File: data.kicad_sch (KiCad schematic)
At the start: 37 parts, among them J3001 Conn_01x04, J6 USB_C_Receptacle_USB2.0, SW1 SWITCH-SPST, SW2 SWITCH-SPST, U27 RP2040, U3 TPS22919DCKR, U8 W25Q16JVUXIQ TR, U9 SK6812, Y1 12MHz

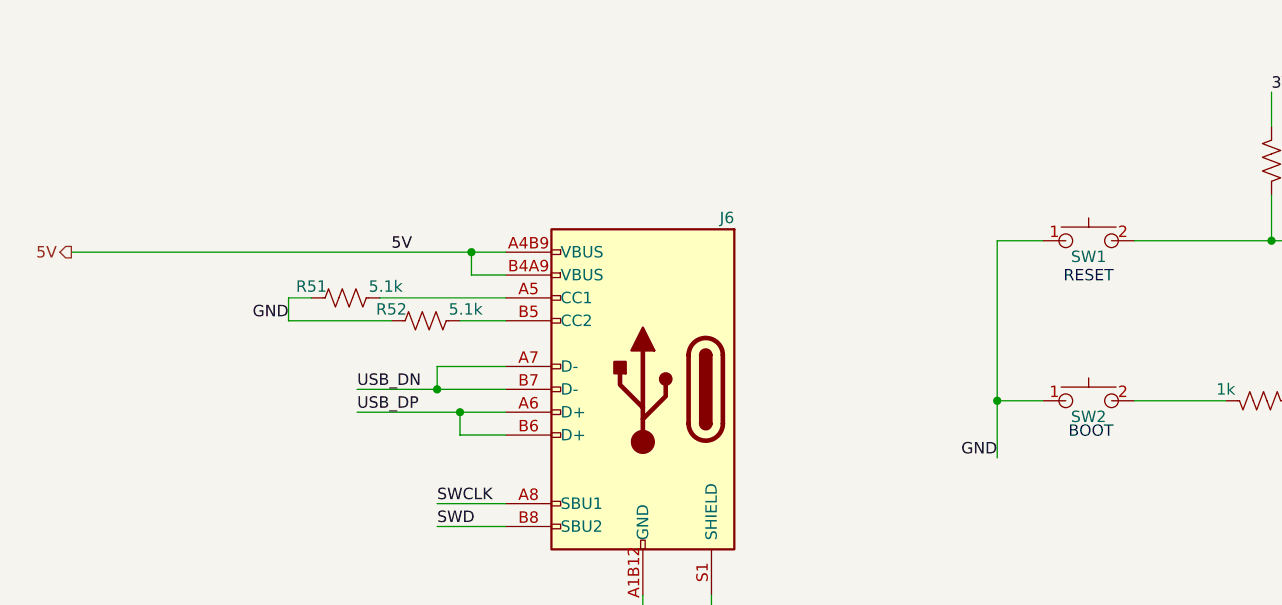
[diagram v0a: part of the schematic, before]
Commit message: started to piece in the BZM2 into schematic
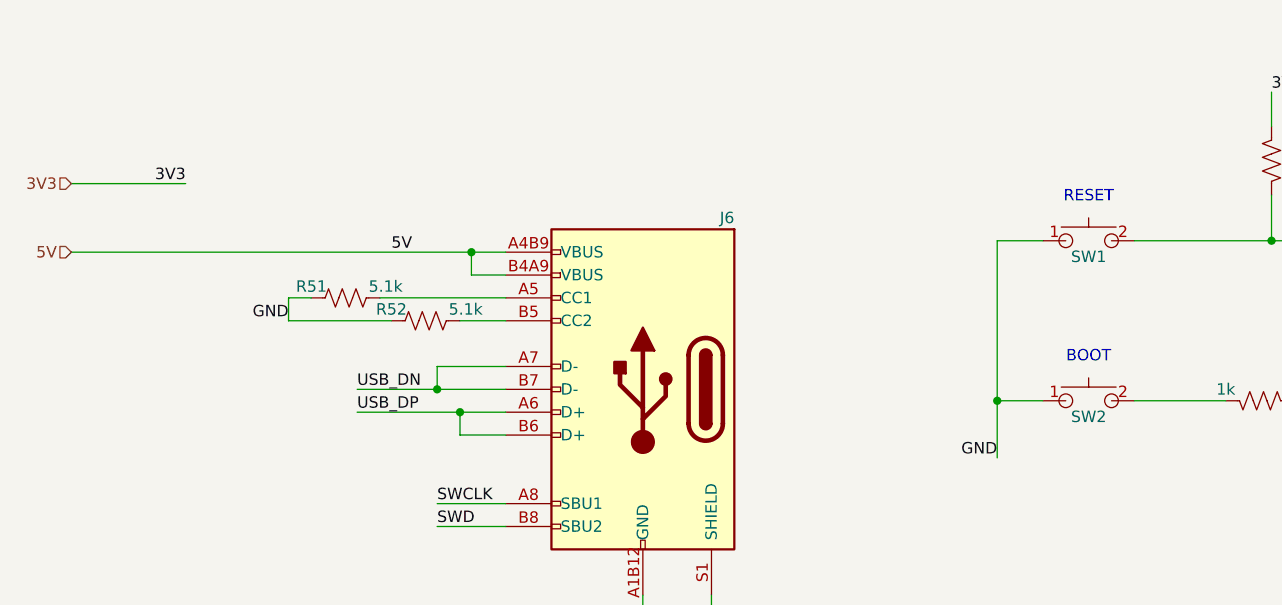
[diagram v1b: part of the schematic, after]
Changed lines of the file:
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@@
 	(text "BOOT"
 		(exclude_from_sim no)
-		(at 164.084 96.266 0)
+		(at 163.83 87.884 0)
 		(effects
 			(font
@@
 	(text "RESET"
 		(exclude_from_sim no)
-		(at 163.83 78.994 0)
+		(at 163.83 70.104 0)
 		(effects
 			(font
@@
 	(wire
 		(pts
+			(xy 50.8 68.58) (xy 63.5 68.58)
+		)
+		(stroke
+			(width 0)
+			(type default)
+		)
+	)
+	(wire
+		(pts
 			(xy 254 48.26) (xy 265.43 48.26)
 		)
@@
 			)
 			(justify left bottom)
+		)
+	)
+	(label "3V3"
+		(at 63.5 68.58 180)
+		(effects
+			(font
+				(size 1.27 1.27)
+			)
+			(justify right bottom)
 		)
 	)
@@
 	)
 	(hierarchical_label "5V"
-		(shape output)
+		(shape input)
 		(at 50.8 76.2 180)
 		(effects
 			(font
+				(size 1.27 1.27)
+			)
+			(justify right)
+		)
+	)
+	(hierarchical_label "3V3"
+		(shape input)
+		(at 50.8 68.58 180)
+		(effects
+			(font

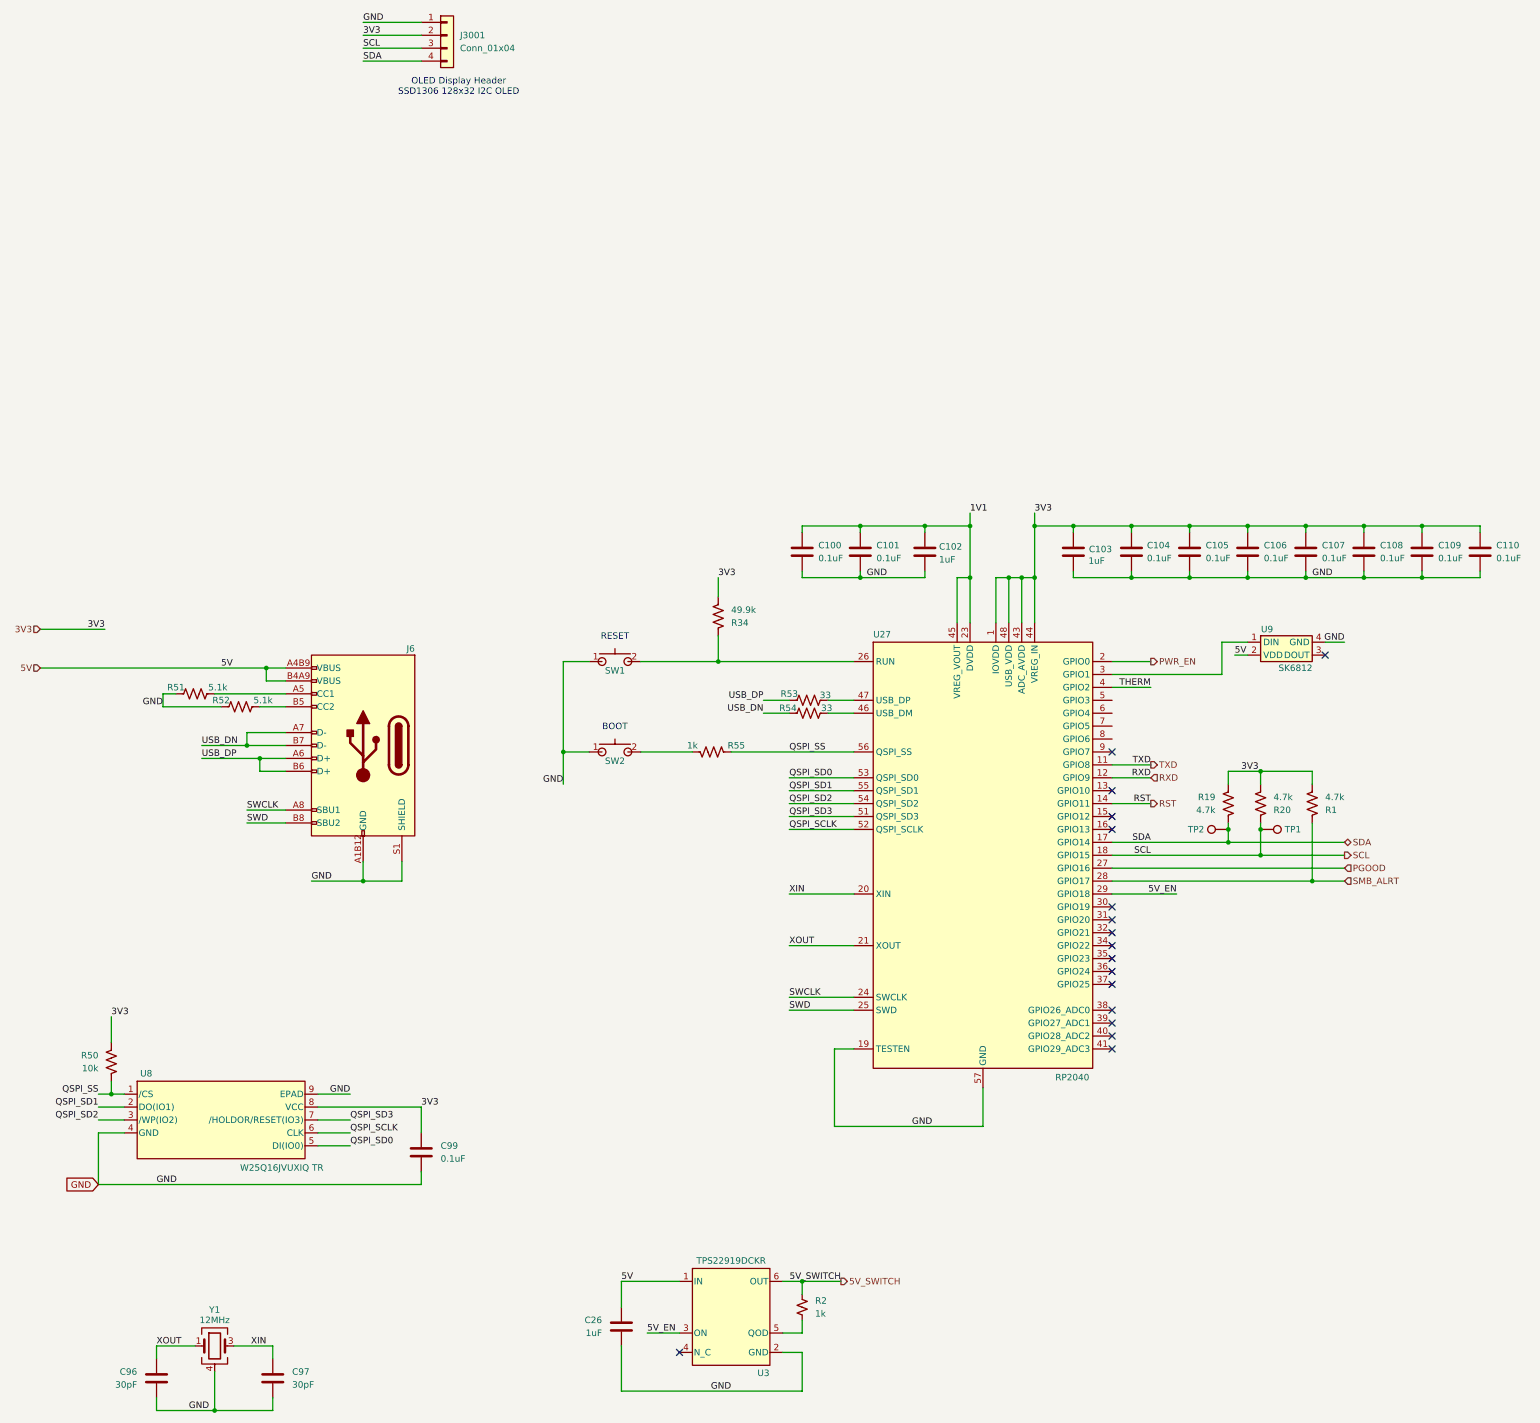
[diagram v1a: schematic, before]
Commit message: finished adding ASICs to schematic. Change VR to single phase 2.8V output
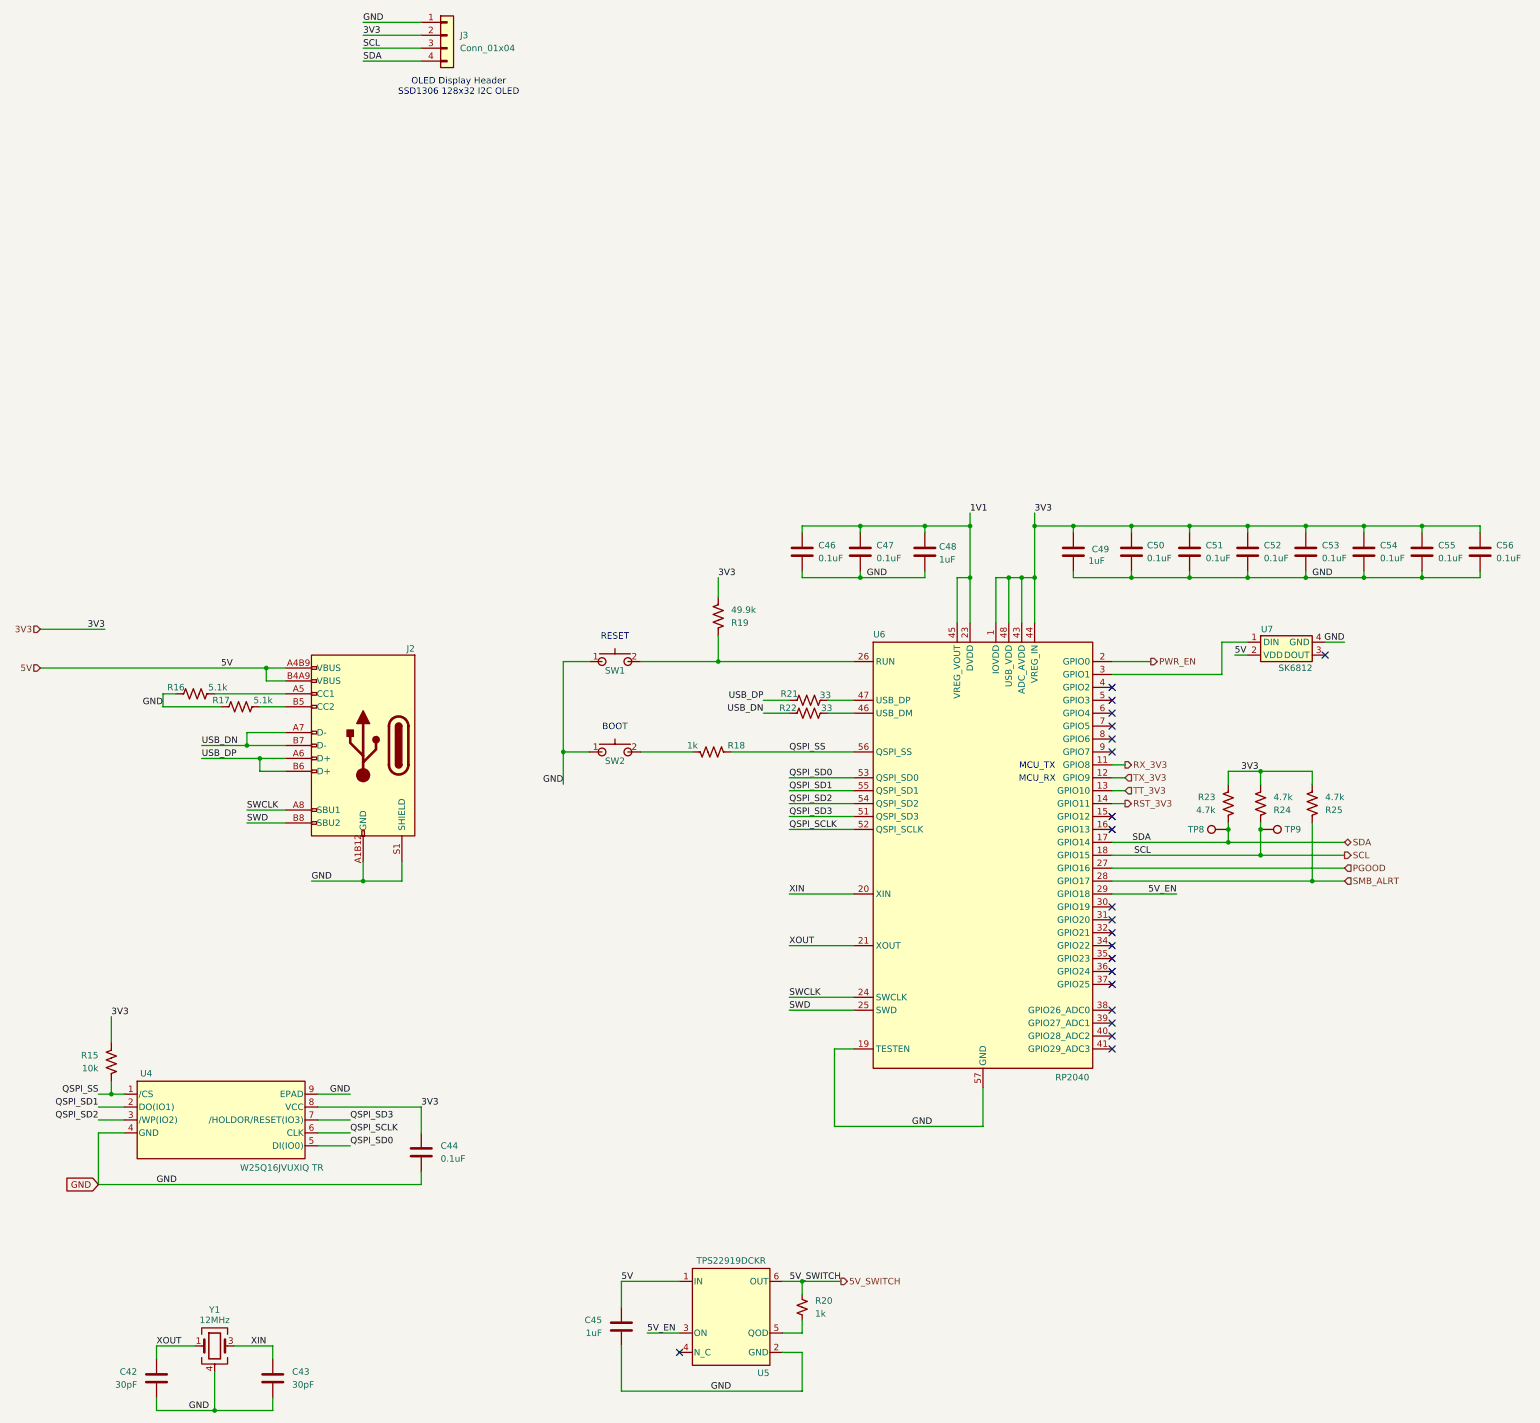
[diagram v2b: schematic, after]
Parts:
- renumbered C96 to C42, C97 to C43, C99 to C44, C26 to C45, C100 to C46, C101 to C47, C102 to C48, C103 to C49, C104 to C50, C105 to C51, C106 to C52, C107 to C53, C108 to C54, C109 to C55, C110 to C56, J6 to J2, J3001 to J3, R50 to R15, R51 to R16, R52 to R17, R55 to R18, R34 to R19, R2 to R20, R53 to R21, R54 to R22, R19 to R23, R20 to R24, R1 to R25, TP2 to TP8, TP1 to TP9, U8 to U4, U3 to U5, U27 to U6, U9 to U7
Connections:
- net TT_3V3: now reaches U6.13 (GPIO10)
- net RST renamed RST_3V3
- net RXD renamed TX_3V3
- net THERM: no longer names the net of U6.4 (GPIO2)
- net TXD renamed RX_3V3
- no-connect marks 17 -> 21
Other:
- note added: "MCU_RX"
- note added: "MCU_TX"

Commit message: switched to smaller level shifter diodes. switched ASIC modes
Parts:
- TP8: value TestPoint -> SDA; footprint TestPoint:TestPoint_Pad_D1.0mm -> bitaxe:TestPoint_Pad_D1.0mm
- TP9: value TestPoint -> SCL; footprint TestPoint:TestPoint_Pad_D1.0mm -> bitaxe:TestPoint_Pad_D1.0mm

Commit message: more routing
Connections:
- net MCU_BOOT: now reaches R18.2, SW2.2
- net MCU_RESET: now reaches R19.1, SW1.2, U6.26 (RUN)
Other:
- moved on the sheet: R18
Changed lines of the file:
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@@
 	(wire
 		(pts
-			(xy 186.69 92.71) (xy 210.82 92.71)
+			(xy 193.04 92.71) (xy 210.82 92.71)
 		)
 		(stroke
@@
 	(wire
 		(pts
-			(xy 179.07 92.71) (xy 168.91 92.71)
+			(xy 185.42 92.71) (xy 168.91 92.71)
 		)
 		(stroke
@@
 		)
 	)
+	(label "MCU_RESET"
+		(at 171.45 74.93 0)
+		(effects
+			(font
+				(size 1.27 1.27)
+			)
+			(justify left bottom)
+		)
+	)
 	(label "GND"
 		(at 80.01 222.25 0)
@@
 		)
 	)
+	(label "MCU_BOOT"
+		(at 171.45 92.71 0)
+		(effects
+			(font
+				(size 1.27 1.27)
+			)
+			(justify left bottom)
+		)
+	)
 	(label "1V1"
 		(at 233.68 45.72 0)
@@
 	(symbol
 		(lib_id "Device:R_US")
-		(at 182.88 92.71 270)
+		(at 189.23 92.71 270)
 		(mirror x)
 		(unit 1)
@@
 		(dnp no)
 		(property "Reference" "R18"
-			(at 187.706 91.44 90)
+			(at 194.056 91.44 90)
 			(effects
 				(font
@@
 		)
 		(property "Value" "1k"
-			(at 179.07 91.44 90)
+			(at 185.42 91.44 90)
 			(effects
 				(font
@@
 		)
 		(property "Footprint" "Resistor_SMD:R_0402_1005Metric"
-			(at 175.26 92.71 0)
+			(at 181.61 92.71 0)
 			(effects
 				(font
@@
 		)
 		(property "Datasheet" ""
-			(at 172.72 92.71 0)
+			(at 179.07 92.71 0)
 			(effects
 				(font
@@
 		)
 		(property "Description" ""
-			(at 182.88 92.71 0)
+			(at 189.23 92.71 0)
 			(effects
 				(font
@@
 		)
 		(property "Manufacturer" ""
-			(at 170.18 92.71 0)
+			(at 176.53 92.71 0)
 			(effects
 				(font
@@
 		)
 		(property "PARTNO" "RC0402FR-071KL"
-			(at 182.88 92.71 0)
+			(at 189.23 92.71 0)
 			(effects
 				(font
@@
 		)
 		(property "DK" "311-1.00KLRCT-ND"
-			(at 182.88 92.71 0)
+			(at 189.23 92.71 0)
 			(effects
 				(font
@@
 		)
 		(property "LCSC" "C106235"
-			(at 182.88 92.71 0)
+			(at 189.23 92.71 0)
 			(effects
 				(font
@@
 		)
 		(property "Field6" ""
-			(at 182.88 92.71 90)
+			(at 189.23 92.71 90)
 			(effects
 				(font
@@
 		)
 		(property "Mouser" ""
-			(at 182.88 92.71 90)
+			(at 189.23 92.71 90)
 			(effects
 				(font
